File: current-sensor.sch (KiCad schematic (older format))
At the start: 36 parts, among them J1 ‎0197134001‎, J2 ‎0197134001‎, J3 0731000105, J4 Molex_SL_01x02_Male, J5 Molex_SL_01x02_Male, SW1 PN12SHNA03QE, SW2 OS103011MA7QP1, SW3 OS103011MA7QP1, U1 ACS730xLCTR-40AB, U2 AD8616xRM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

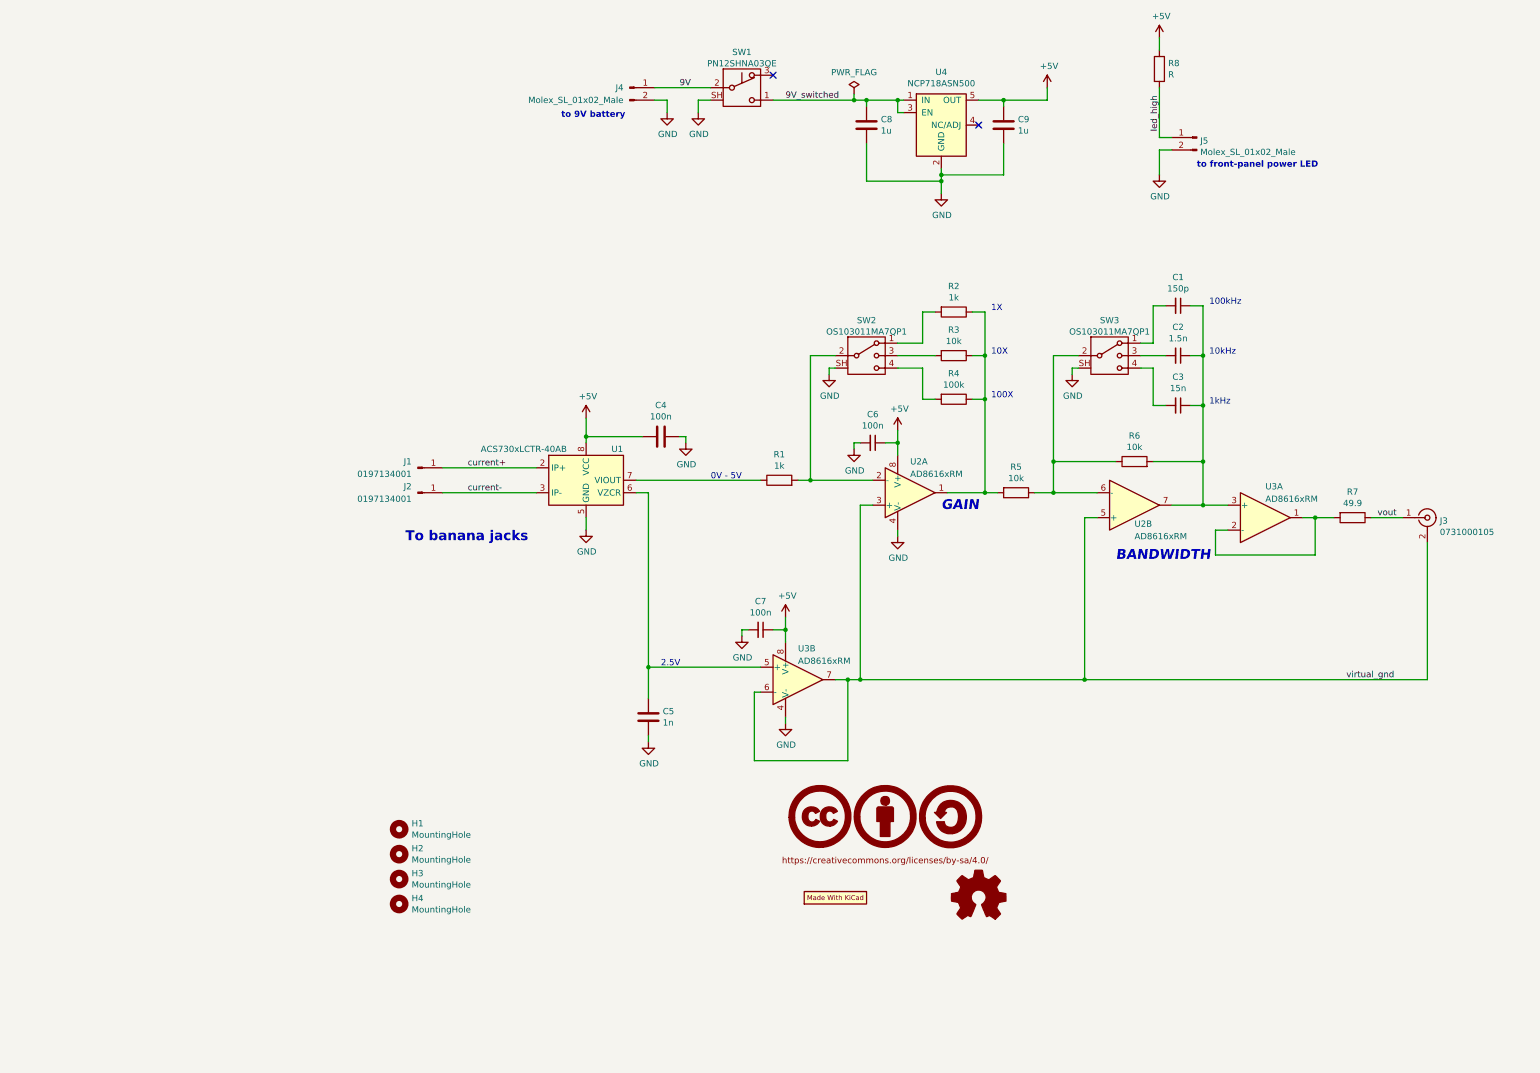
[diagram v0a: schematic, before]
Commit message: add power flag to GND and add PDF schematic
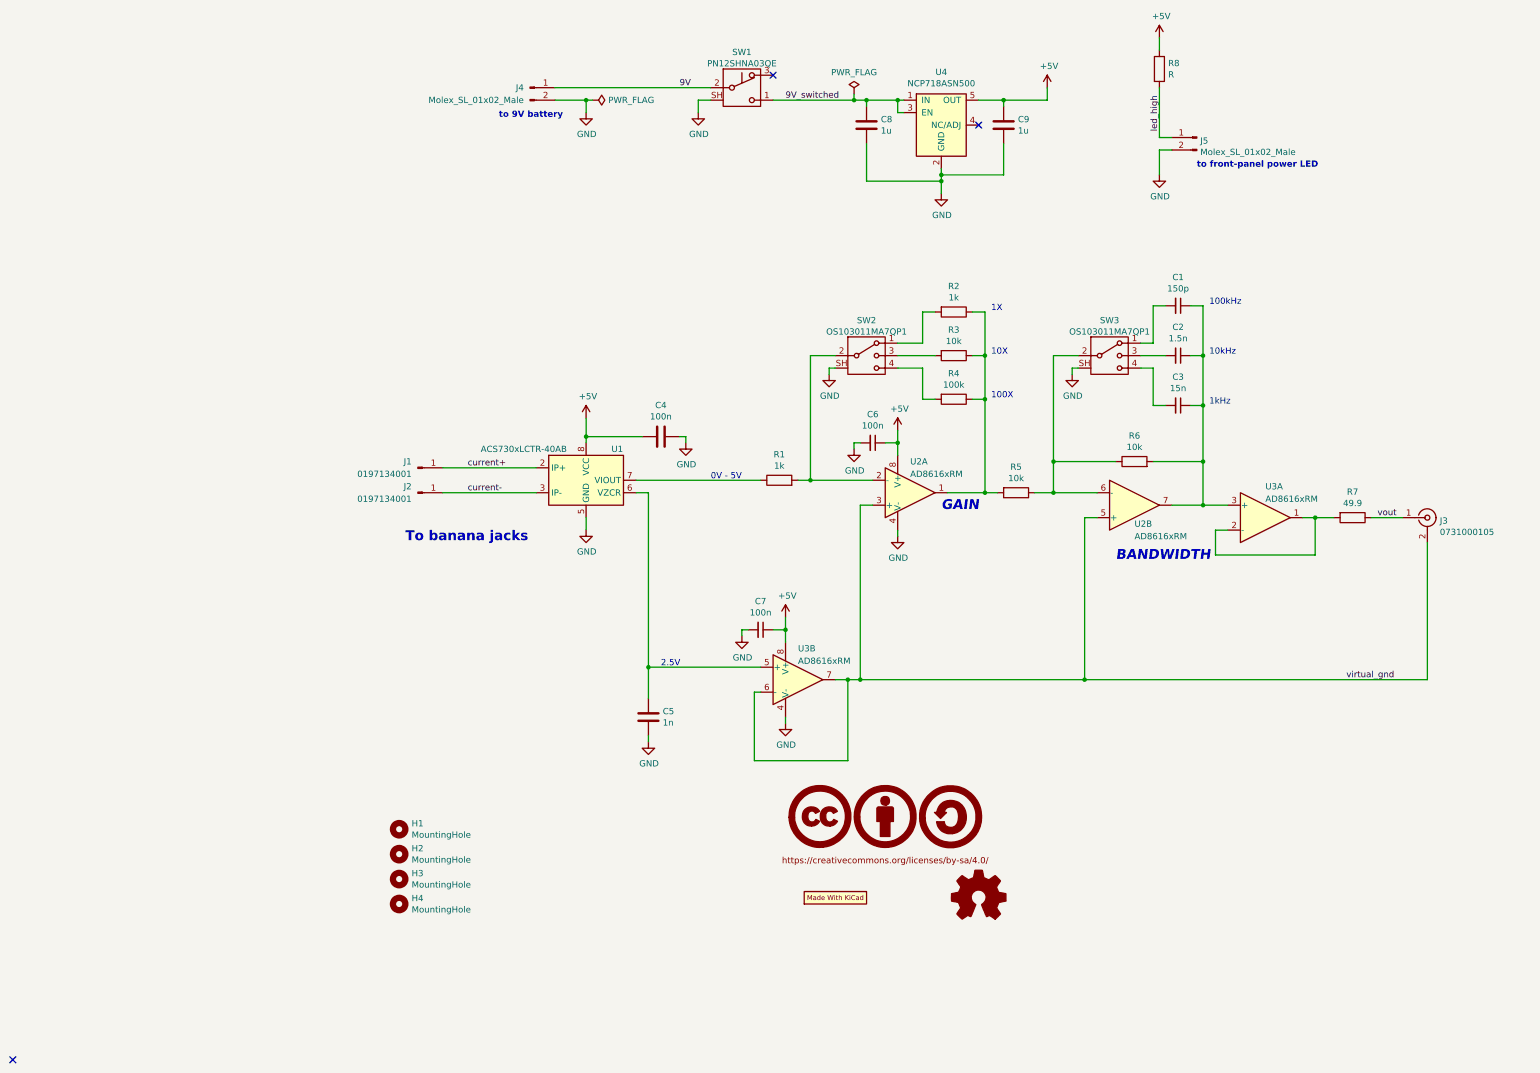
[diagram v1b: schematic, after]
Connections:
- no-connect marks 2 -> 3
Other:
- moved on the sheet: J4
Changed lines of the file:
@@
 L power:GND #PWR0103
 U 1 1 5EFC0FA6
-P 3250 1400
-F 0 "#PWR0103" H 3250 1150 50  0001 C CNN
-F 1 "GND" H 3255 1227 50  0000 C CNN
-F 2 "" H 3250 1400 50  0001 C CNN
-F 3 "" H 3250 1400 50  0001 C CNN
-	1    3250 1400
-	1    0    0    -1
-$EndComp
-Wire Wire Line
-	3250 1400 3250 1300
-Wire Wire Line
-	3250 1300 3150 1300
+P 2600 1400
+F 0 "#PWR0103" H 2600 1150 50  0001 C CNN
+F 1 "GND" H 2605 1227 50  0000 C CNN
+F 2 "" H 2600 1400 50  0001 C CNN
+F 3 "" H 2600 1400 50  0001 C CNN
+	1    2600 1400
+	1    0    0    -1
+$EndComp
 $Comp
 L Device:C C8
@@
 NoConn ~ 4100 1100
 Wire Wire Line
-	3150 1200 3600 1200
+	2350 1200 3600 1200
 Connection ~ 4750 1300
 $Comp
@@
 Text Notes 7500 1850 0    50   ~ 10
 to front-panel power LED
-Text Notes 2400 1450 0    50   ~ 10
+Text Notes 1900 1450 0    50   ~ 10
 to 9V battery
 $Comp
@@
 L Connector_gkeeth:Molex_SL_01x02_Male J4
 U 1 1 5EFBA6AD
-P 2950 1200
-F 0 "J4" H 2900 1200 50  0000 R CNN
-F 1 "Molex_SL_01x02_Male" H 2900 1100 50  0000 R CNN
-F 2 "Connector_Molex_SL:Molex_SL_A-70543-0001_1x02_P2.54mm_Vertical" H 2950 1200 50  0001 C CNN
-F 3 "https://www.molex.com/pdm_docs/sd/705430001_sd.pdf" H 2950 1200 50  0001 C CNN
-	1    2950 1200
-	1    0    0    -1
-$EndComp
+P 2150 1200
+F 0 "J4" H 2100 1200 50  0000 R CNN
+F 1 "Molex_SL_01x02_Male" H 2100 1100 50  0000 R CNN
+F 2 "Connector_Molex_SL:Molex_SL_A-70543-0001_1x02_P2.54mm_Vertical" H 2150 1200 50  0001 C CNN
+F 3 "https://www.molex.com/pdm_docs/sd/705430001_sd.pdf" H 2150 1200 50  0001 C CNN
+	1    2150 1200
+	1    0    0    -1
+$EndComp
+NoConn ~ -2000 9000
+$Comp
+L power:PWR_FLAG #FLG0102
+U 1 1 5F4DA91F
+P 2650 1300
+F 0 "#FLG0102" H 2650 1375 50  0001 C CNN
+F 1 "PWR_FLAG" V 2650 1428 50  0000 L CNN
+F 2 "" H 2650 1300 50  0001 C CNN
+F 3 "~" H 2650 1300 50  0001 C CNN
+	1    2650 1300
+	0    1    1    0
+$EndComp
+Wire Wire Line
+	2600 1300 2350 1300
+Wire Wire Line
+	2600 1400 2600 1300
+Connection ~ 2600 1300
+Wire Wire Line
+	2650 1300 2600 1300
 $EndSCHEMATC

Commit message: swap 100kHz and 1kHz bandwidth positions
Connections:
- net at C1.2: now also SW3.4; no longer SW3.1
- net at C3.2: now also SW3.1; no longer SW3.4
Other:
- moved on the sheet: C1, C3
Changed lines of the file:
@@
 Sheet 1 1
 Title "Current Sensor"
-Date "2020-08-24"
+Date "2020-10-17"
 Rev "0"
 Comp "G. Keeth"
@@
 L Device:C_Small C1
 U 1 1 5EFE9D19
-P 7350 2950
-F 0 "C1" V 7121 2950 50  0000 C CNN
-F 1 "150p" V 7212 2950 50  0000 C CNN
-F 2 "Capacitor_SMD:C_0603_1608Metric" H 7350 2950 50  0001 C CNN
-F 3 "~" H 7350 2950 50  0001 C CNN
-	1    7350 2950
+P 7350 3750
+F 0 "C1" V 7121 3750 50  0000 C CNN
+F 1 "150p" V 7212 3750 50  0000 C CNN
+F 2 "Capacitor_SMD:C_0603_1608Metric" H 7350 3750 50  0001 C CNN
+F 3 "~" H 7350 3750 50  0001 C CNN
+	1    7350 3750
 	0    1    1    0
 $EndComp
@@
 L Device:C_Small C3
 U 1 1 5EFEA97C
-P 7350 3750
-F 0 "C3" V 7121 3750 50  0000 C CNN
-F 1 "15n" V 7212 3750 50  0000 C CNN
-F 2 "Capacitor_SMD:C_0603_1608Metric" H 7350 3750 50  0001 C CNN
-F 3 "~" H 7350 3750 50  0001 C CNN
-	1    7350 3750
+P 7350 2950
+F 0 "C3" V 7121 2950 50  0000 C CNN
+F 1 "15n" V 7212 2950 50  0000 C CNN
+F 2 "Capacitor_SMD:C_0603_1608Metric" H 7350 2950 50  0001 C CNN
+F 3 "~" H 7350 2950 50  0001 C CNN
+	1    7350 2950
 	0    1    1    0
 $EndComp
@@
 Text Notes 5850 3700 0    50   ~ 0
 100X
-Text Notes 7600 2950 0    50   ~ 0
+Text Notes 7600 3750 0    50   ~ 0
 100kHz
 Text Notes 7600 3350 0    50   ~ 0
 10kHz
-Text Notes 7600 3750 0    50   ~ 0
+Text Notes 7600 2950 0    50   ~ 0
 1kHz
 Wire Wire Line

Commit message: Change hall effect sensor to +/-20A
binding posts are limited to 15A. Decrease hall effect sensor range to
lowest available (+/-20A).

It is possible to use the equivalent part with a higher current range,
but the connectors would need to be modified and the overall system gain
would decrease due to reduced sensor sensitivity.
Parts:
- removed U1: ACS730xLCTR-40AB, Package_SO:SOIC-8_3.9x4.9mm_P1.27mm, symbol Sensor_Current:ACS730xLCTR-40AB
- added U1: ACS730xLCTR-20AB, Package_SO:SOIC-8_3.9x4.9mm_P1.27mm, symbol Sensor_Current:ACS730xLCTR-20AB
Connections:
- net +5V: now also U1.8 (VCC)
- net GND: now also U1.5 (GND)
- net current+: now also U1.1 (IP+), U1.2 (IP+)
- net current-: now also U1.3 (IP-), U1.4 (IP-)
- net at C5.1, U3.5 (+): now also U1.6 (VZCR)
- net at R1.1: now also U1.7 (VIOUT)
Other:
- note added: "+/- 20A"
- note added: "100mV/A"
- note added: "gain x 100mV/A"
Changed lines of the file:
@@
 Wire Wire Line
 	7200 1200 7200 1600
-$Comp
-L Sensor_Current:ACS730xLCTR-40AB U1
-U 1 1 5F43380D
-P 2600 4350
-F 0 "U1" H 2850 4600 50  0000 C CNN
-F 1 "ACS730xLCTR-40AB" H 2100 4600 50  0000 C CNN
-F 2 "Package_SO:SOIC-8_3.9x4.9mm_P1.27mm" H 2950 4250 50  0001 L CIN
-F 3 "http://www.allegromicro.com/~/media/Files/Datasheets/ACS730-Datasheet.ashx?la=en" H 2600 4350 50  0001 C CNN
-	1    2600 4350
-	1    0    0    -1
-$EndComp
 Wire Wire Line
 	4100 1300 4750 1300
@@
 Wire Wire Line
 	2650 1300 2600 1300
+$Comp
+L Sensor_Current:ACS730xLCTR-20AB U1
+U 1 1 5F8C5B53
+P 2600 4350
+F 0 "U1" H 2850 4600 50  0000 C CNN
+F 1 "ACS730xLCTR-20AB" H 2100 4600 50  0000 C CNN
+F 2 "Package_SO:SOIC-8_3.9x4.9mm_P1.27mm" H 2950 4250 50  0001 L CIN
+F 3 "http://www.allegromicro.com/~/media/Files/Datasheets/ACS730-Datasheet.ashx?la=en" H 2600 4350 50  0001 C CNN
+	1    2600 4350
+	1    0    0    -1
+$EndComp
+Text Notes 3600 4450 0    50   ~ 0
+100mV/A
+Text Notes 1650 4350 0    50   ~ 0
++/- 20A
+Text Notes 9450 4900 0    50   ~ 0
+gain x 100mV/A
 $EndSCHEMATC

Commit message: adjust planes around current connectors and add silk
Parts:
- C8, C9: footprint Capacitor_SMD:C_0603_1608Metric -> Capacitor_SMD:C_0805_2012Metric
- R8: value R -> 3.3k
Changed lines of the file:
@@
 F 0 "C8" H 4965 1546 50  0000 L CNN
 F 1 "1u" H 4965 1455 50  0000 L CNN
-F 2 "Capacitor_SMD:C_0603_1608Metric" H 4888 1350 50  0001 C CNN
+F 2 "Capacitor_SMD:C_0805_2012Metric" H 4888 1350 50  0001 C CNN
 F 3 "~" H 4850 1500 50  0001 C CNN
 	1    4850 1500
@@
 P 7200 1050
 F 0 "R8" H 7270 1096 50  0000 L CNN
-F 1 "R" H 7270 1005 50  0000 L CNN
+F 1 "3.3k" H 7270 1005 50  0000 L CNN
 F 2 "Resistor_SMD:R_0603_1608Metric" V 7130 1050 50  0001 C CNN
 F 3 "~" H 7200 1050 50  0001 C CNN
@@
 F 0 "C9" H 6065 1546 50  0000 L CNN
 F 1 "1u" H 6065 1455 50  0000 L CNN
-F 2 "Capacitor_SMD:C_0603_1608Metric" H 5988 1350 50  0001 C CNN
+F 2 "Capacitor_SMD:C_0805_2012Metric" H 5988 1350 50  0001 C CNN
 F 3 "~" H 5950 1500 50  0001 C CNN
 	1    5950 1500

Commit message: revision 1 of current sensor
- fix gain/bandwidth switch pin numbering
- move faston connectors further apart
- switch from MSOP to SOIC package for op-amp
- add silk labels to switches and connectors
- reduce LED resistor to increase brightness
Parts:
- R8: value 3.3k -> 2.2k
- U2, U3: footprint Package_SO:MSOP-8_3x3mm_P0.65mm -> Package_SO:SOIC-8_3.9x4.9mm_P1.27mm
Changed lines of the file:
@@
 Sheet 1 1
 Title "Current Sensor"
-Date "2020-10-17"
-Rev "0"
+Date "2020-12-07"
+Rev "1"
 Comp "G. Keeth"
 Comment1 ""
@@
 F 0 "U3" H 8050 4900 50  0000 L CNN
 F 1 "AD8616xRM" H 8050 4800 50  0000 L CNN
-F 2 "Package_SO:MSOP-8_3x3mm_P0.65mm" H 8150 4650 50  0001 C CNN
+F 2 "Package_SO:SOIC-8_3.9x4.9mm_P1.27mm" H 8150 4650 50  0001 C CNN
 F 3 "https://www.analog.com/media/en/technical-documentation/data-sheets/AD8615_8616_8618.pdf" H 8300 4800 50  0001 C CNN
 	1    8050 4650
@@
 P 7200 1050
 F 0 "R8" H 7270 1096 50  0000 L CNN
-F 1 "3.3k" H 7270 1005 50  0000 L CNN
+F 1 "2.2k" H 7270 1005 50  0000 L CNN
 F 2 "Resistor_SMD:R_0603_1608Metric" V 7130 1050 50  0001 C CNN
 F 3 "~" H 7200 1050 50  0001 C CNN
@@
 F 0 "U2" H 7000 4700 50  0000 L CNN
 F 1 "AD8616xRM" H 7000 4800 50  0000 L CNN
-F 2 "Package_SO:MSOP-8_3x3mm_P0.65mm" H 7100 4550 50  0001 C CNN
+F 2 "Package_SO:SOIC-8_3.9x4.9mm_P1.27mm" H 7100 4550 50  0001 C CNN
 F 3 "https://www.analog.com/media/en/technical-documentation/data-sheets/AD8615_8616_8618.pdf" H 7250 4700 50  0001 C CNN
 	2    7000 4550
@@
 F 0 "U2" H 5200 4200 50  0000 L CNN
 F 1 "AD8616xRM" H 5200 4300 50  0000 L CNN
-F 2 "Package_SO:MSOP-8_3x3mm_P0.65mm" H 5300 4450 50  0001 C CNN
+F 2 "Package_SO:SOIC-8_3.9x4.9mm_P1.27mm" H 5300 4450 50  0001 C CNN
 F 3 "https://www.analog.com/media/en/technical-documentation/data-sheets/AD8615_8616_8618.pdf" H 5450 4600 50  0001 C CNN
 	1    5200 4450
@@
 F 0 "U3" H 4300 6200 50  0000 L CNN
 F 1 "AD8616xRM" H 4300 6100 50  0000 L CNN
-F 2 "Package_SO:MSOP-8_3x3mm_P0.65mm" H 4400 5950 50  0001 C CNN
+F 2 "Package_SO:SOIC-8_3.9x4.9mm_P1.27mm" H 4400 5950 50  0001 C CNN
 F 3 "https://www.analog.com/media/en/technical-documentation/data-sheets/AD8615_8616_8618.pdf" H 4550 6100 50  0001 C CNN
 	2    4300 5950
@@
 F 0 "U2" H 5158 4496 50  0001 L CNN
 F 1 "AD8616xRM" H 5158 4405 50  0001 L CNN
-F 2 "Package_SO:MSOP-8_3x3mm_P0.65mm" H 5200 4450 50  0001 C CNN
+F 2 "Package_SO:SOIC-8_3.9x4.9mm_P1.27mm" H 5200 4450 50  0001 C CNN
 F 3 "https://www.analog.com/media/en/technical-documentation/data-sheets/AD8615_8616_8618.pdf" H 5350 4600 50  0001 C CNN
 	3    5100 4450
@@
 F 0 "U3" H 4258 5996 50  0001 L CNN
 F 1 "AD8616xRM" H 4258 5905 50  0001 L CNN
-F 2 "Package_SO:MSOP-8_3x3mm_P0.65mm" H 4300 5950 50  0001 C CNN
+F 2 "Package_SO:SOIC-8_3.9x4.9mm_P1.27mm" H 4300 5950 50  0001 C CNN
 F 3 "https://www.analog.com/media/en/technical-documentation/data-sheets/AD8615_8616_8618.pdf" H 4450 6100 50  0001 C CNN
 	3    4200 5950
